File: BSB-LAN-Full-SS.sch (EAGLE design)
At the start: 120 parts, among them IC1 LAN8710A-EZC, IC2 TPS2376DDA, IC3 TX4138, IC4 SY8089AAAC, IC6 CH340X, Q1 BC847, Q2 BC857, Q3 BC847, Q4 WPM2015-3/TR, Q5 BC847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

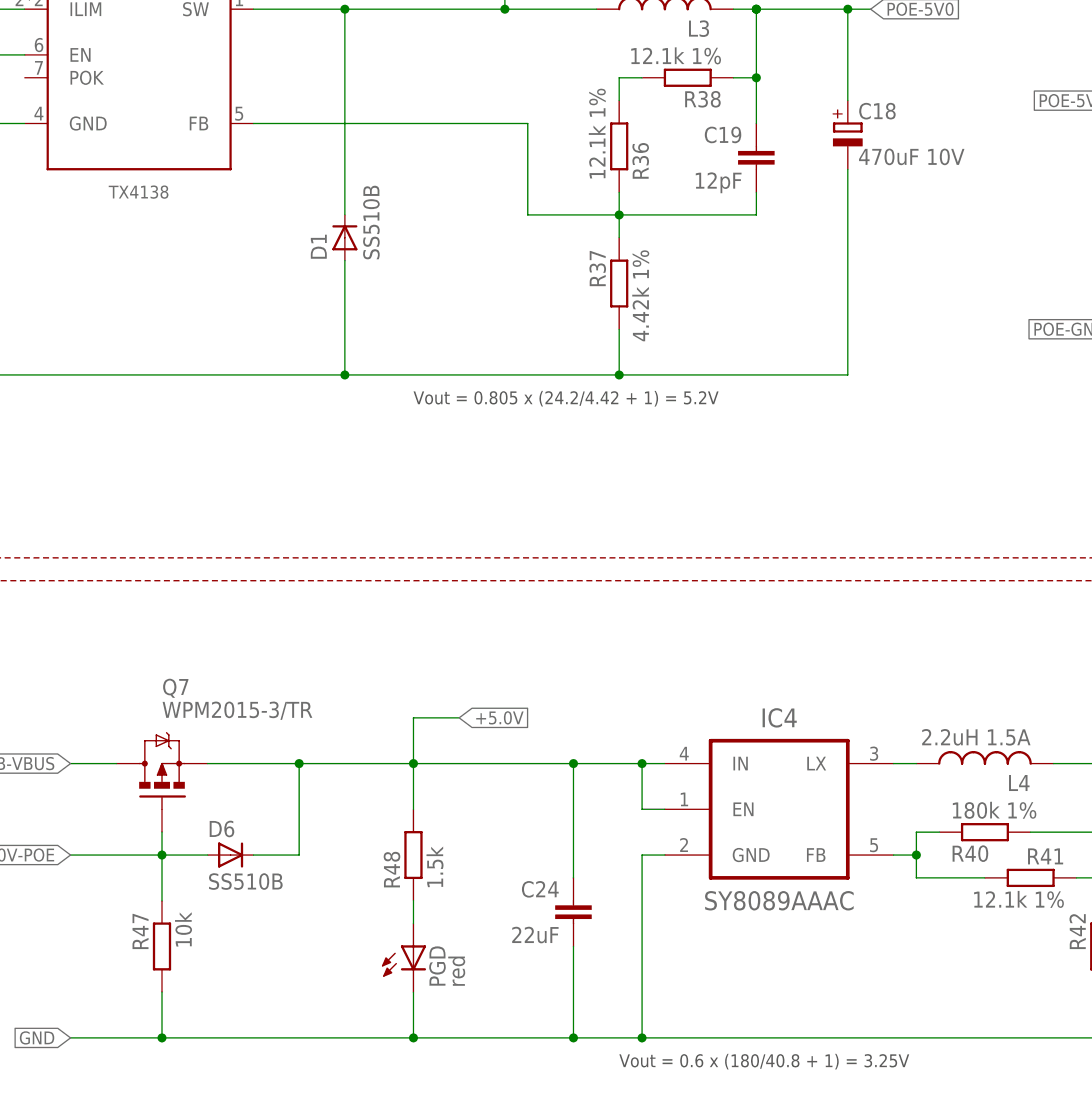
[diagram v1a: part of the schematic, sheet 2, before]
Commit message: Annotate Alternate Parts for Full S-S design
Some parts can have alternative compatible PNs.
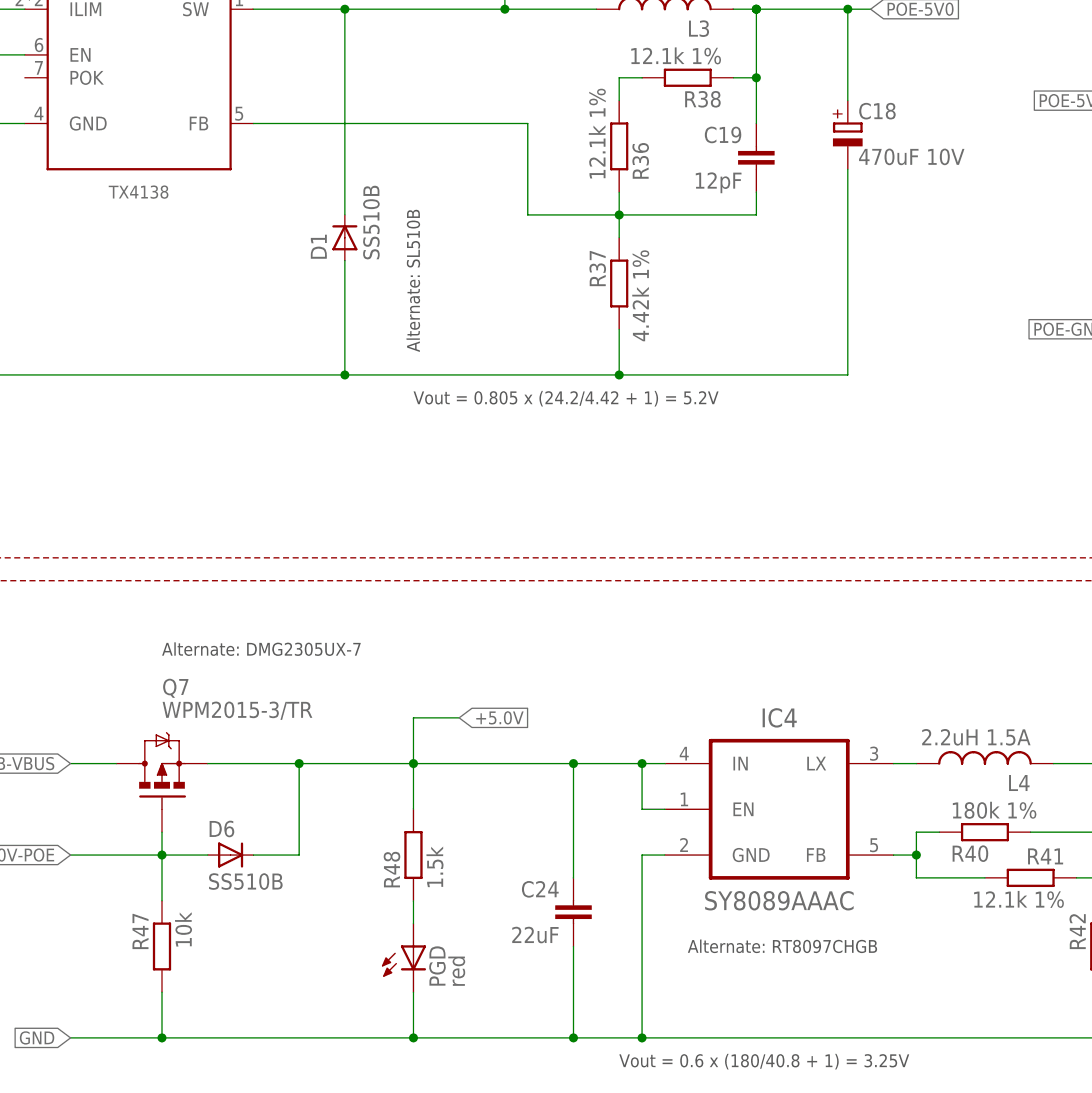
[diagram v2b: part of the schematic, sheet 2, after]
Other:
- note added: "Alternate: DMG2305UX-7"
- note added: "Alternate: RT8097CHGB"
- note added: "Alternate: SL510B"
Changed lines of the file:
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@@
 <text x="88.9" y="116.84" size="1.4224" layer="97" font="vector" ratio="10" align="center-left">Vout = 0.805 x (24.2/4.42 + 1) = 5.2V</text>
 <text x="111.76" y="43.18" size="1.4224" layer="97" font="vector" ratio="10" align="center-left">Vout = 0.6 x (180/40.8 + 1) = 3.25V</text>
+<text x="119.38" y="55.88" size="1.4224" layer="97" font="vector" ratio="10" align="center-left">Alternate: RT8097CHGB</text>
+<text x="60.96" y="88.9" size="1.4224" layer="97" font="vector" ratio="10" align="center-left">Alternate: DMG2305UX-7</text>
+<text x="88.9" y="121.92" size="1.4224" layer="97" font="vector" ratio="10" rot="R90" align="center-left">Alternate: SL510B</text>
 </plain>
 <instances>

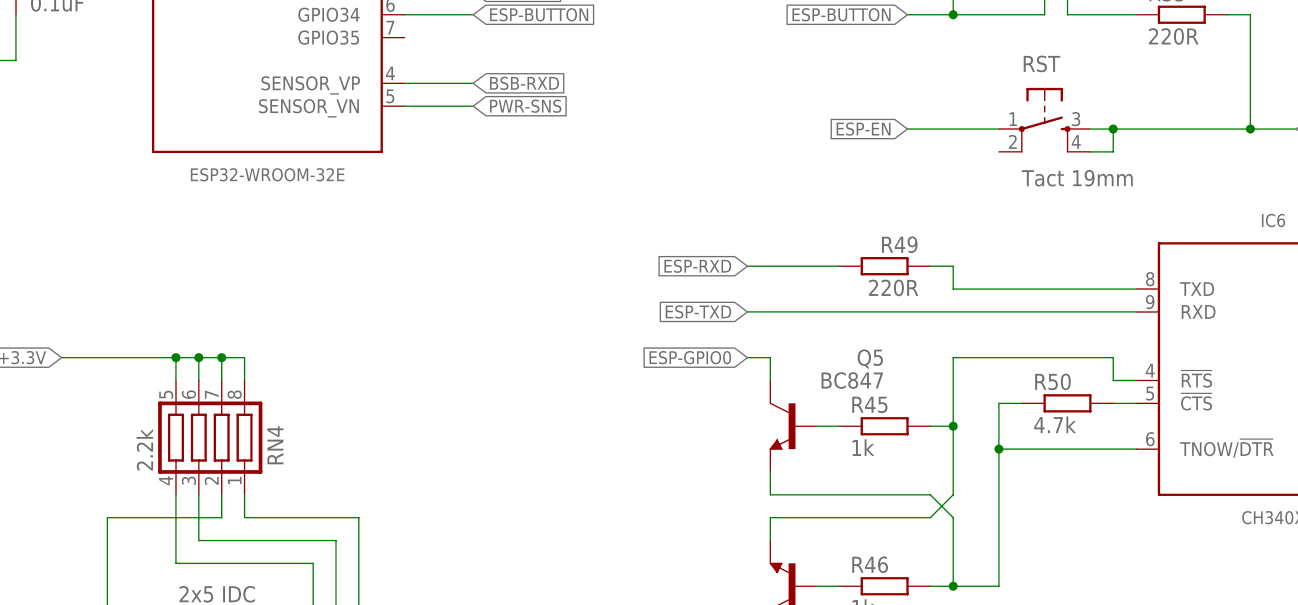
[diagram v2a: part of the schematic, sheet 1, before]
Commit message: Correct ESP32 Prog Control + Update Libraries
1. Correct the control of automatic bootloader entry by adding missing resistor from GPIO2 to GPIO0.
2. Update libraries and fix layout to account for changes.
3. Change the LAN versions of the boards to use the ESP32 with external antenna. If the PCB antenna is used then it is not possible to get the PCB into the enclosure because components stick out on both ends!
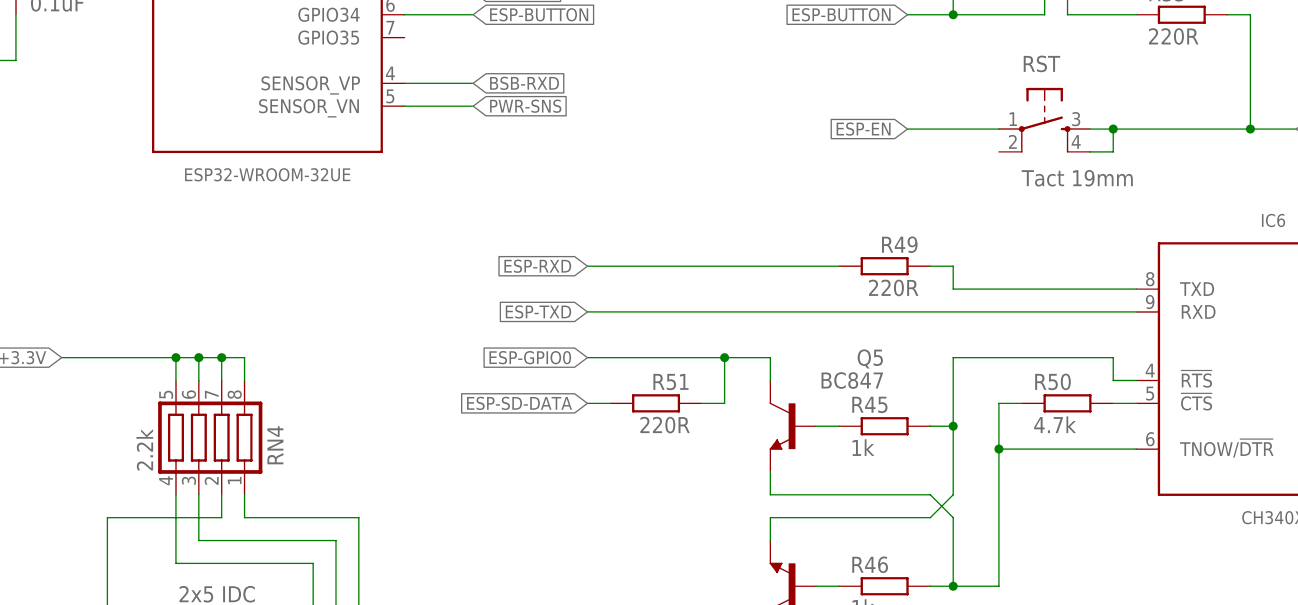
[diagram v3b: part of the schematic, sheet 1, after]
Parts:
- added R51: 220R, BSB-LAN:R-EU_R0402
- ESP1: value ESP32-WROOM-32E -> ESP32-WROOM-32UE; device BSB-LAN:ESP32-WROOM-32E -> BSB-LAN:ESP32-WROOM-32UE
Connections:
- net ESP-GPIO0: now also R51.1
- net ESP-SD-DATA: now also R51.2
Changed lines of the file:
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@@
 <schematic xreflabel="%F%N/%S.%C%R" xrefpart="/%S.%C%R">
 <attributes>
-<attribute name="REVISION" value="v1.0"/>
+<attribute name="REVISION" value="v1.1"/>
 </attributes>
 <variantdefs>
@@
 </part>
 <part name="IC4" library="BSB-LAN" deviceset="SY8089*?C" device="AA" technology="A"/>
-<part name="ESP1" library="BSB-LAN" deviceset="ESP32-WROOM" device="-32E"/>
+<part name="ESP1" library="BSB-LAN" deviceset="ESP32-WROOM" device="-32UE" value="ESP32-WROOM-32UE"/>
 <part name="USD" library="BSB-LAN" deviceset="MICROSD" device="" value="XKTF-001A"/>
 <part name="C1" library="BSB-LAN" deviceset="C-EU" device="C0603" value="2.2uF">
@@
 <part name="RN4" library="BSB-LAN" deviceset="R-NET-04" device="-R1206" value="2.2k">
 <attribute name="LCSC_PART" value="C414564"/>
+</part>
+<part name="R51" library="BSB-LAN" deviceset="R-EU_" device="R0402" value="220R">
+<attribute name="LCSC_PART" value="C25091"/>
 </part>
 </parts>
@@
 <instance part="RN4" gate="G$1" x="55.88" y="43.18" rot="MR90">
 <attribute name="LCSC_PART" x="55.88" y="43.18" size="1.4224" layer="96" font="vector" ratio="10" rot="MR90" align="center" display="off"/>
+</instance>
+<instance part="R51" gate="G$1" x="104.14" y="48.26" rot="MR0">
+<attribute name="LCSC_PART" x="104.14" y="48.26" size="1.4224" layer="96" font="vector" ratio="10" align="center" display="off"/>
 </instance>
 </instances>
@@
 <junction x="187.96" y="121.92"/>
 </segment>
+<segment>
+<wire x1="99.06" y1="48.26" x2="96.52" y2="48.26" width="0.1524" layer="91"/>
+<label x="96.52" y="48.26" size="1.4224" layer="95" font="vector" ratio="10" rot="MR0" xref="yes"/>
+<pinref part="R51" gate="G$1" pin="2"/>
+</segment>
 </net>
 <net name="ESP-SD-CLK" class="4">
@@
 <net name="ESP-GPIO0" class="4">
 <segment>
-<wire x1="116.84" y1="53.34" x2="114.3" y2="53.34" width="0.1524" layer="91"/>
-<label x="114.3" y="53.34" size="1.4224" layer="95" font="vector" ratio="10" rot="R180" xref="yes"/>
+<wire x1="116.84" y1="53.34" x2="111.76" y2="53.34" width="0.1524" layer="91"/>
+<label x="96.52" y="53.34" size="1.4224" layer="95" font="vector" ratio="10" rot="R180" xref="yes"/>
 <pinref part="Q5" gate="G$1" pin="C"/>
+<wire x1="111.76" y1="53.34" x2="96.52" y2="53.34" width="0.1524" layer="91"/>
 <wire x1="116.84" y1="50.8" x2="116.84" y2="53.34" width="0.1524" layer="91"/>
+<pinref part="R51" gate="G$1" pin="1"/>
+<wire x1="109.22" y1="48.26" x2="111.76" y2="48.26" width="0.1524" layer="91"/>
+<wire x1="111.76" y1="48.26" x2="111.76" y2="53.34" width="0.1524" layer="91"/>
+<junction x="111.76" y="53.34"/>
 </segment>
 <segment>
@@
 </segment>
 <segment>
-<wire x1="157.48" y1="58.42" x2="114.3" y2="58.42" width="0.1524" layer="91"/>
-<label x="114.3" y="58.42" size="1.4224" layer="95" font="vector" ratio="10" rot="MR0" xref="yes"/>
+<wire x1="157.48" y1="58.42" x2="96.52" y2="58.42" width="0.1524" layer="91"/>
+<label x="96.52" y="58.42" size="1.4224" layer="95" font="vector" ratio="10" rot="MR0" xref="yes"/>
 <pinref part="IC6" gate="G$1" pin="RXD"/>
 </segment>
@@
 </segment>
 <segment>
-<wire x1="124.46" y1="63.5" x2="114.3" y2="63.5" width="0.1524" layer="91"/>
-<label x="114.3" y="63.5" size="1.4224" layer="95" font="vector" ratio="10" rot="MR0" xref="yes"/>
+<wire x1="124.46" y1="63.5" x2="96.52" y2="63.5" width="0.1524" layer="91"/>
+<label x="96.52" y="63.5" size="1.4224" layer="95" font="vector" ratio="10" rot="MR0" xref="yes"/>
 <pinref part="R49" gate="G$1" pin="2"/>
 </segment>
